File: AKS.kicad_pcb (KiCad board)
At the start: 2 copper layers, 29 x 63.5 mm, 13 parts, among them J1 Power, J10 JETSON_CAN, J2 Relay board, J3 JETSON DC JACK, J4 Jetson 40-pin GPIO, J5 BTS7960 H-bridge (signals onl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, J9 VESC_CAN, U1 SN65HVD230, U2 Polulu D24V10F5 (12 to 5V con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

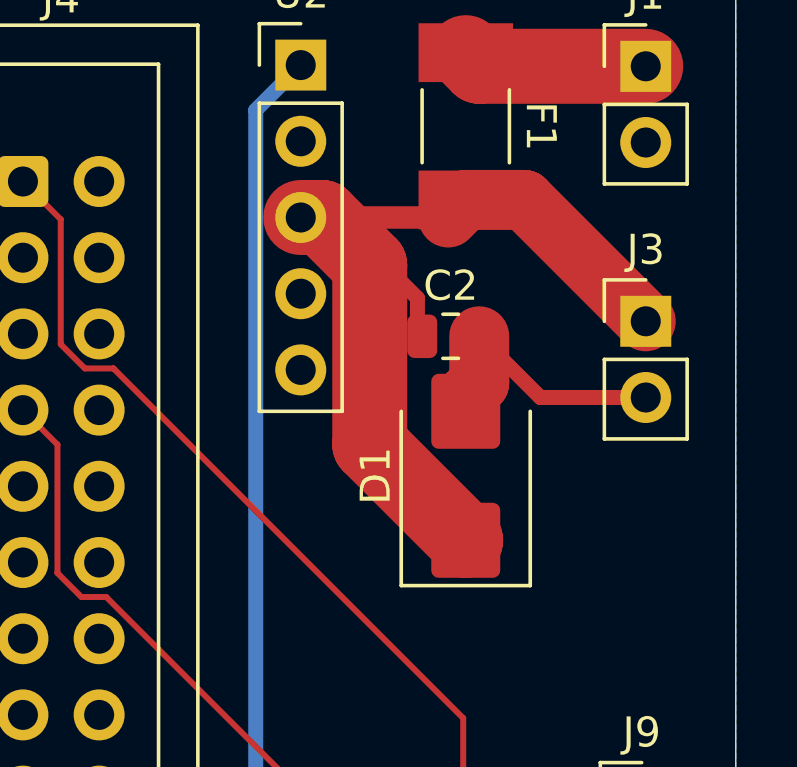
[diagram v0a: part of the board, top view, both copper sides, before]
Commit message: Add files via upload
Adjusted the width of Cu traces to accommodate the high-current from +12V
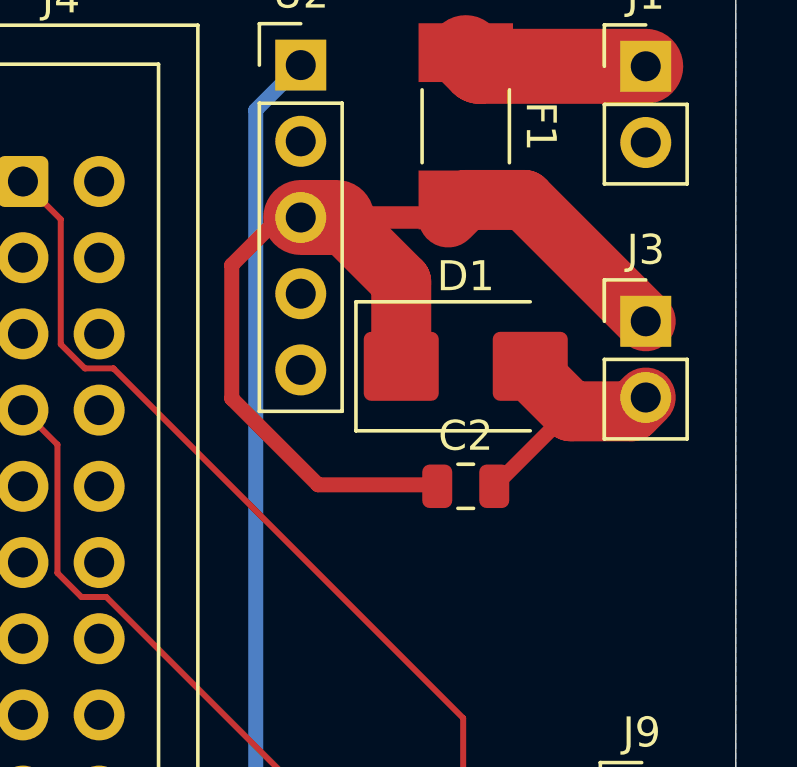
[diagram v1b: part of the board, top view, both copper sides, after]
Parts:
- J5: value BTS7960 H-bridge (signals only) -> BTS7960 H-bridge
- moved C2 5.02 mm to (91.0, 116.0)
- moved D1 3.65 mm to (91.0, 112.0), turned to 0 degrees
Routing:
- net /+12V_SAFE: track 33.1 -> 35.9 mm
- net /GND: track 66.8 -> 68.7 mm
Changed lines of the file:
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@@
 		(capping no)
 		(filling no)
-		(zone_defaults)
 		(pcbplotparams
 			(layerselection 0x00000000_00000000_55555555_5755f5ff)
@@
 			)
 		)
-		(property "Value" "BTS7960 H-bridge (signals only)"
+		(property "Value" "BTS7960 H-bridge "
 			(at 0 20.16 0)
 			(layer "F.Fab")
@@
 	(footprint "Capacitor_SMD:C_0805_2012Metric"
 		(layer "F.Cu")
-		(at 90.5 111)
+		(at 91 116)
 		(descr "Capacitor SMD 0805 (2012 Metric), square (rectangular) end terminal, IPC-7351 nominal, (Body size source: IPC-SM-782 page 76, https://www.pcb-3d.com/wordpress/wp-content/uploads/ipc-sm-782a_amendment_1_and_2.pdf, https://docs.google.com/spreadsheets/d/1BsfQQcO9C6DZCsRaXUlFlo91Tg2WpOkGARC1WS5S8t0/edit?usp=sharing)")
 		(tags "capacitor")
@@
 	(footprint "Diode_SMD:D_SMB"
 		(layer "F.Cu")
-		(at 91 115.65 90)
+		(at 91 112)
 		(descr "Diode SMB (DO-214AA)")
 		(tags "Diode SMB (DO-214AA)")
 		(property "Reference" "D1"
-			(at 0 -3 90)
+			(at 0 -3 0)
 			(layer "F.SilkS")
 			(effects
@@
 		)
 		(property "Value" "SMBJ15A TVS diode (12 input transient suppresion)"
-			(at 0 3.1 90)
+			(at 0 3.1 0)
 			(layer "F.Fab")
 			(effects
@@
 		)
 		(property "Datasheet" ""
-			(at 0 0 90)
+			(at 0 0 0)
 			(unlocked yes)
 			(layer "F.Fab")
@@
 		)
 		(property "Description" "Bidirectional transient-voltage-suppression diode"
-			(at 0 0 90)
+			(at 0 0 0)
 			(unlocked yes)
 			(layer "F.Fab")
@@
 		(fp_line
 			(start -3.66 -2.15)
-			(end 2.15 -2.15)
+			(end -3.66 2.15)
 			(stroke
 				(width 0.12)
@@
 		(fp_line
 			(start -3.66 -2.15)
-			(end -3.66 2.15)
+			(end 2.15 -2.15)
 			(stroke
 				(width 0.12)
@@
 		)
 		(fp_line
-			(start 3.65 -2.25)
-			(end 3.65 2.25)
+			(start -3.65 -2.25)
+			(end 3.65 -2.25)
 			(stroke
 				(width 0.05)
@@
 		)
 		(fp_line
-			(start -3.65 -2.25)
-			(end 3.65 -2.25)
+			(start -3.65 2.25)
+			(end -3.65 -2.25)
 			(stroke
 				(width 0.05)
@@
 		)
 		(fp_line
-			(start 3.65 2.25)
-			(end -3.65 2.25)
+			(start 3.65 -2.25)
+			(end 3.65 2.25)
 			(stroke
 				(width 0.05)
@@
 		)
 		(fp_line
-			(start -3.65 2.25)
-			(end -3.65 -2.25)
+			(start 3.65 2.25)
+			(end -3.65 2.25)
 			(stroke
 				(width 0.05)
@@
 		)
 		(fp_line
-			(start 2.3 -2)
+			(start -2.3 2)
 			(end -2.3 -2)
 			(stroke
@@
 		)
 		(fp_line
-			(start 2.3 -2)
-			(end 2.3 2)
+			(start -0.64944 -0.79908)
+			(end -0.64944 0.80112)
 			(stroke
 				(width 0.1)
@@
 		)
 		(fp_line
-			(start -0.64944 -0.79908)
-			(end -0.64944 0.80112)
+			(start -0.64944 0.00102)
+			(end -1.55114 0.00102)
 			(stroke
 				(width 0.1)
@@
 		)
 		(fp_line
-			(start 0.50118 0.00102)
-			(end 1.4994 0.00102)
+			(start -0.64944 0.00102)
+			(end 0.50118 -0.79908)
 			(stroke
 				(width 0.1)
@@
 		(fp_line
 			(start -0.64944 0.00102)
-			(end 0.50118 -0.79908)
+			(end 0.50118 0.75032)
 			(stroke
 				(width 0.1)
@@
 		)
 		(fp_line
-			(start -0.64944 0.00102)
-			(end -1.55114 0.00102)
+			(start 0.50118 0.00102)
+			(end 1.4994 0.00102)
 			(stroke
 				(width 0.1)
@@
 		)
 		(fp_line
-			(start -0.64944 0.00102)
-			(end 0.50118 0.75032)
+			(start 0.50118 0.75032)
+			(end 0.50118 -0.79908)
 			(stroke
 				(width 0.1)
@@
 		)
 		(fp_line
-			(start 0.50118 0.75032)
-			(end 0.50118 -0.79908)
+			(start 2.3 -2)
+			(end -2.3 -2)
 			(stroke
 				(width 0.1)
@@
 		)
 		(fp_line
-			(start 2.3 2)
-			(end -2.3 2)
+			(start 2.3 -2)
+			(end 2.3 2)
 			(stroke
 				(width 0.1)
@@
 		)
 		(fp_line
-			(start -2.3 2)
-			(end -2.3 -2)
+			(start 2.3 2)
+			(end -2.3 2)
 			(stroke
 				(width 0.1)
@@
 		)
 		(fp_text user "${REFERENCE}"
-			(at 0 -3 90)
+			(at 0 -3 0)
 			(layer "F.Fab")
 			(effects
@@
 		)
 		(pad "1" smd roundrect
-			(at -2.15 0 90)
+			(at -2.15 0)
 			(size 2.5 2.3)
 			(layers "F.Cu" "F.Mask" "F.Paste")
@@
 		)
 		(pad "2" smd roundrect
-			(at 2.15 0 90)
+			(at 2.15 0)
 			(size 2.5 2.3)
 			(layers "F.Cu" "F.Mask" "F.Paste")
@@
 	)
 	(segment
-		(start 89.38891 110.8)
-		(end 89.5 110.8)
+		(start 83.2 113.072692)
+		(end 86.077308 115.95)
 		(width 0.5)
 		(layer "F.Cu")
@@
 	)
 	(segment
-		(start 90.98891 117.8)
-		(end 87.8 114.61109)
-		(width 2.5)
-		(layer "F.Cu")
-		(net "/+12V_SAFE")
-	)
-	(segment
 		(start 90.415 107.04)
 		(end 85.5 107.04)
@@
 	)
 	(segment
-		(start 85.5 107.04)
-		(end 86.702081 107.04)
-		(width 0.5)
+		(start 92.955 106.455)
+		(end 97 110.5)
+		(width 2)
 		(layer "F.Cu")
 		(net "/+12V_SAFE")
 	)
 	(segment
-		(start 91 117.8)
-		(end 90.98891 117.8)
-		(width 2.5)
+		(start 88.85 109.187919)
+		(end 86.702081 107.04)
+		(width 2)
 		(layer "F.Cu")
 		(net "/+12V_SAFE")
 	)
 	(segment
-		(start 92.955 106.455)
-		(end 97 110.5)
+		(start 88.85 112)
+		(end 88.85 109.187919)
 		(width 2)
 		(layer "F.Cu")
@@
 	)
 	(segment
-		(start 86.702081 107.04)
-		(end 88.331041 108.668959)
+		(start 83.2 108.627308)
+		(end 83.2 113.072692)
 		(width 0.5)
 		(layer "F.Cu")
@@
 	)
 	(segment
-		(start 91 106.455)
-		(end 92.955 106.455)
-		(width 2)
-		(layer "F.Cu")
-		(net "/+12V_SAFE")
-	)
-	(segment
-		(start 87.8 108.627308)
-		(end 86.212692 107.04)
+		(start 86.702081 107.04)
+		(end 85.5 107.04)
 		(width 2.5)
 		(layer "F.Cu")
@@
 	)
 	(segment
-		(start 87.8 114.61109)
-		(end 87.8 108.627308)
-		(width 2.5)
+		(start 84.787308 107.04)
+		(end 83.2 108.627308)
+		(width 0.5)
 		(layer "F.Cu")
 		(net "/+12V_SAFE")
 	)
 	(segment
-		(start 86.212692 107.04)
-		(end 85.5 107.04)
-		(width 2.5)
+		(start 91 106.455)
+		(end 92.955 106.455)
+		(width 2)
 		(layer "F.Cu")
 		(net "/+12V_SAFE")
 	)
 	(segment
-		(start 88.331041 108.668959)
-		(end 89.38891 109.726829)
+		(start 86.077308 115.95)
+		(end 90 115.95)
 		(width 0.5)
 		(layer "F.Cu")
@@
 	)
 	(segment
-		(start 89.38891 109.726829)
-		(end 89.38891 110.8)
+		(start 85.5 107.04)
+		(end 84.787308 107.04)
 		(width 0.5)
 		(layer "F.Cu")
@@
 	)
 	(segment
+		(start 93.15 112)
+		(end 93.15 112.15)
+		(width 2)
+		(layer "F.Cu")
+		(net "/GND")
+	)
+	(segment
 		(start 91.96 139.114448)
 		(end 91.96 132.944448)
@@
 	)
 	(segment
+		(start 94.5 113.5)
+		(end 96.54 113.5)
+		(width 2)
+		(layer "F.Cu")
+		(net "/GND")
+	)
+	(segment
 		(start 91.96 132.944448)
 		(end 92.815 132.089448)
@@
 	)
 	(segment
-		(start 91.45 112.55)
-		(end 91.45 111)
-		(width 2)
-		(layer "F.Cu")
-		(net "/GND")
-	)
-	(segment
 		(start 93.23 141.359447)
 		(end 93.23 144.064448)
@@
 	)
 	(segment
-		(start 91 113.5)
-		(end 91 113)
-		(width 2)
+		(start 91.95 116)
+		(end 94.91 113.04)
+		(width 0.5)
 		(layer "F.Cu")
 		(net "/GND")
 	)
 	(segment
-		(start 93.49 113.04)
+		(start 96.54 113.5)
 		(end 97 113.04)
-		(width 0.5)
+		(width 2)
 		(layer "F.Cu")
 		(net "/GND")
@@
 	)
 	(segment
-		(start 95.17 146.979447)
-		(end 95.17 143.048896)
-		(width 0.2)
+		(start 94.91 113.04)
+		(end 97 113.04)
+		(width 0.5)
 		(layer "F.Cu")
 		(net "/GND")
 	)
 	(segment
-		(start 91.96 139.114448)
-		(end 91.96 140.089447)
+		(start 95.17 146.979447)
+		(end 95.17 143.048896)
 		(width 0.2)
 		(layer "F.Cu")
@@
 	)
 	(segment
-		(start 95.429448 142.789448)
-		(end 96.110552 142.789448)
-		(width 0.2)
+		(start 93.15 112.15)
+		(end 94.5 113.5)
+		(width 2)
 		(layer "F.Cu")
 		(net "/GND")
 	)
 	(segment
-		(start 91 113)
-		(end 91.45 112.55)
-		(width 2)
+		(start 91.96 139.114448)
+		(end 91.96 140.089447)
+		(width 0.2)
 		(layer "F.Cu")
 		(net "/GND")
 	)
 	(segment
-		(start 91.45 111)
-		(end 93.49 113.04)
-		(width 0.5)
+		(start 95.429448 142.789448)
+		(end 96.110552 142.789448)
+		(width 0.2)
 		(layer "F.Cu")
 		(net "/GND")

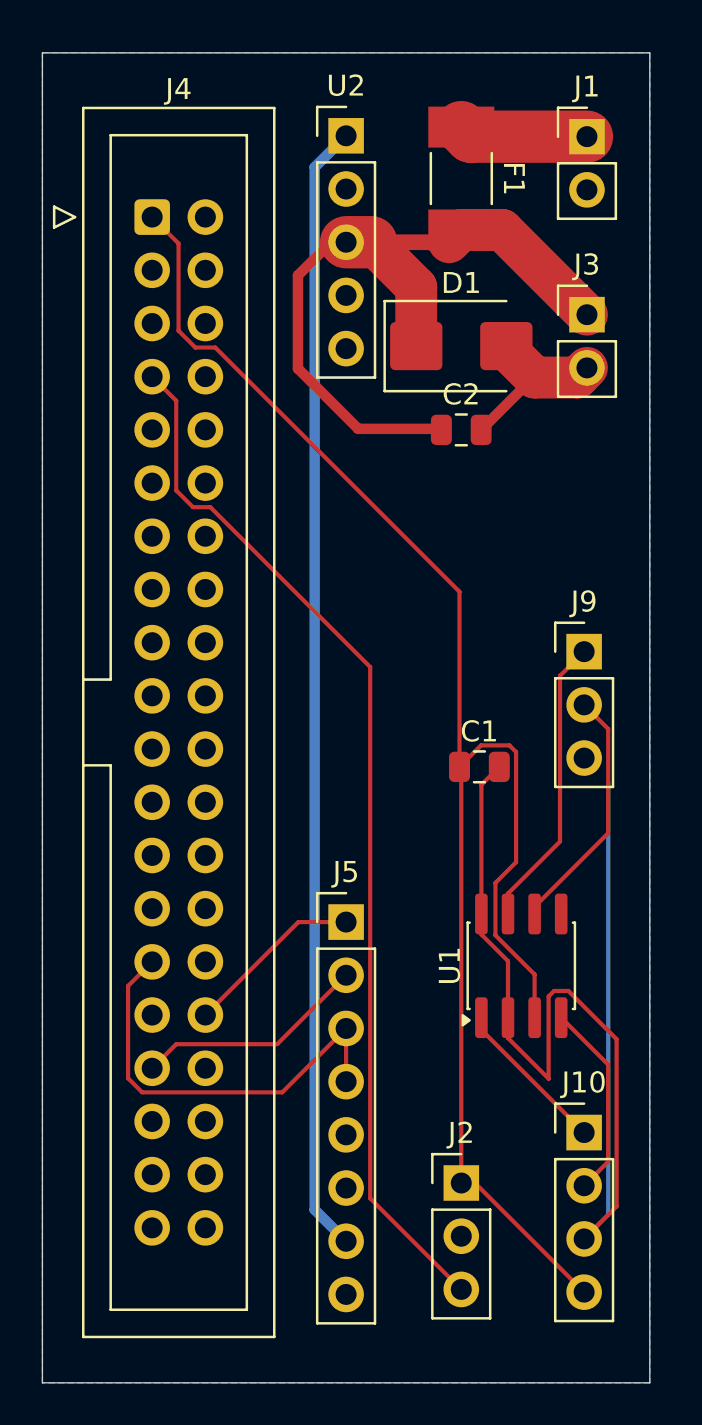
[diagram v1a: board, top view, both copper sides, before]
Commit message: Adjusted the width of Cu traces
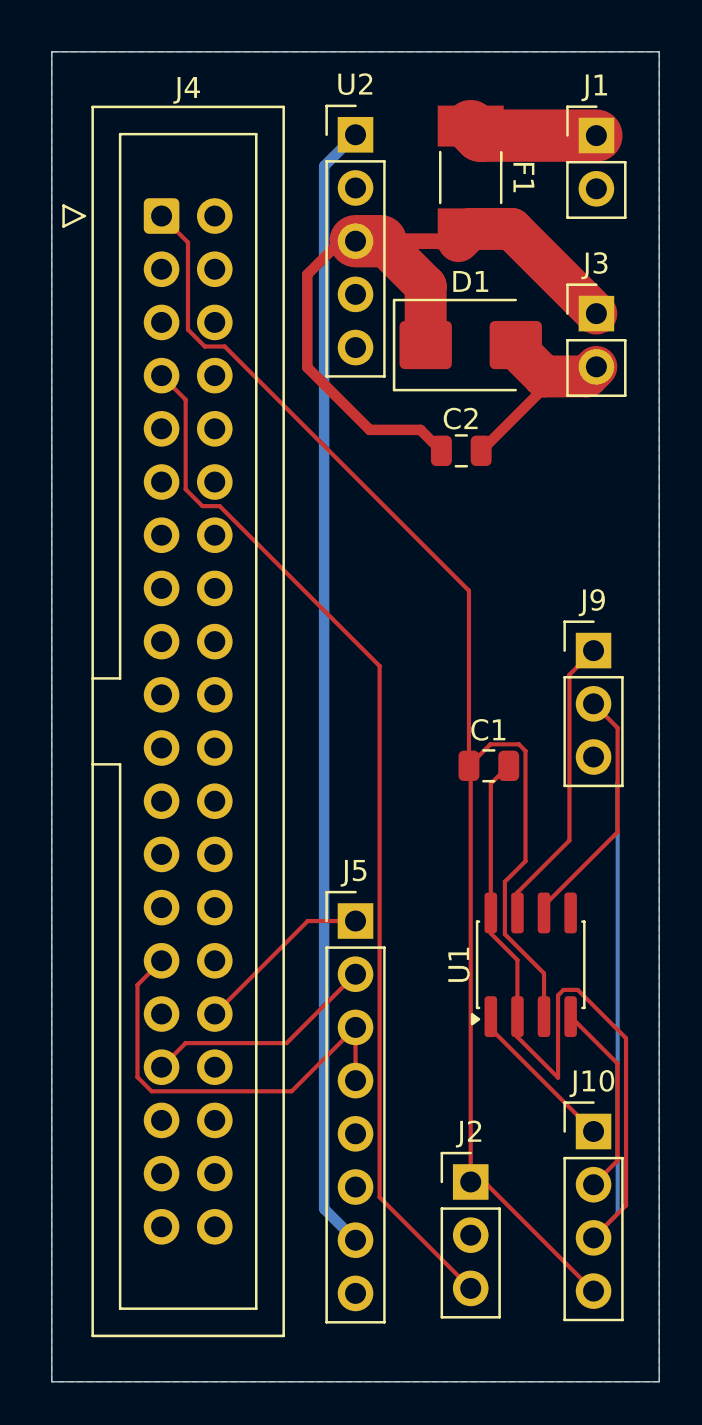
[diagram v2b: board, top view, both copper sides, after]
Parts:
- J5: value BTS7960 H-bridge -> BTS7960 H-bridge (signals only)
- moved C2 1.00 mm to (91.0, 117.0)
- moved C1 0.45 mm to (92.3, 132.0)
- moved J10 0.45 mm to (97.3, 149.5)
- moved J2 0.45 mm to (91.5, 151.9)
- moved J5 0.45 mm to (86.0, 139.4)
- moved J9 0.45 mm to (97.3, 126.5)
- moved U1 0.45 mm to (94.3, 141.5)
- moved D1 0.45 mm to (91.5, 112.0)
- moved F1 0.45 mm to (91.5, 104.0)
- moved J1 0.45 mm to (97.5, 102.0)
- moved J3 0.45 mm to (97.5, 110.5)
- moved J4 0.45 mm to (76.7, 105.8)
- moved U2 0.45 mm to (86.0, 101.9)
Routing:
- net /GND: track 68.7 -> 69.6 mm
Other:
- board text added: "C2"
